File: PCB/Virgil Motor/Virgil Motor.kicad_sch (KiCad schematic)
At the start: 14 parts, among them J1 10056847-101LF, J2 Conn_01x04_Pin, U1 B103, U2 DRV8220DSG, U3 IQS227B00400008TSR, U5 XIAO-RP2350-SMD

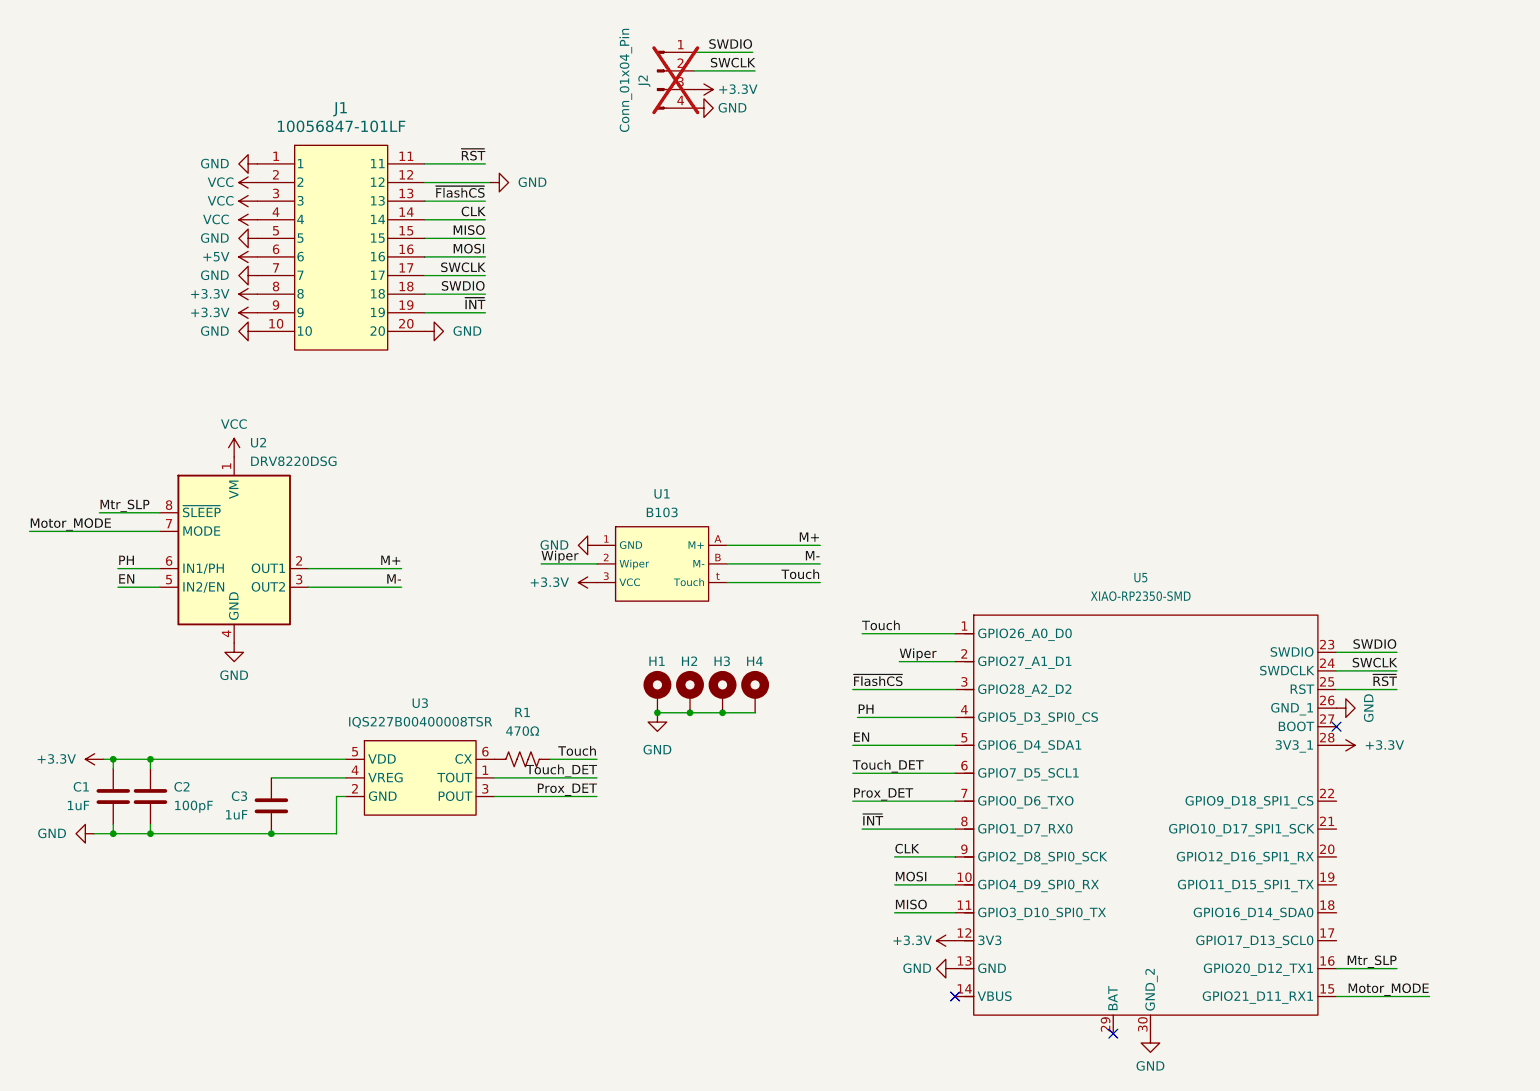
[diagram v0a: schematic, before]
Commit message: Updated PCBs to use raw rp2040s
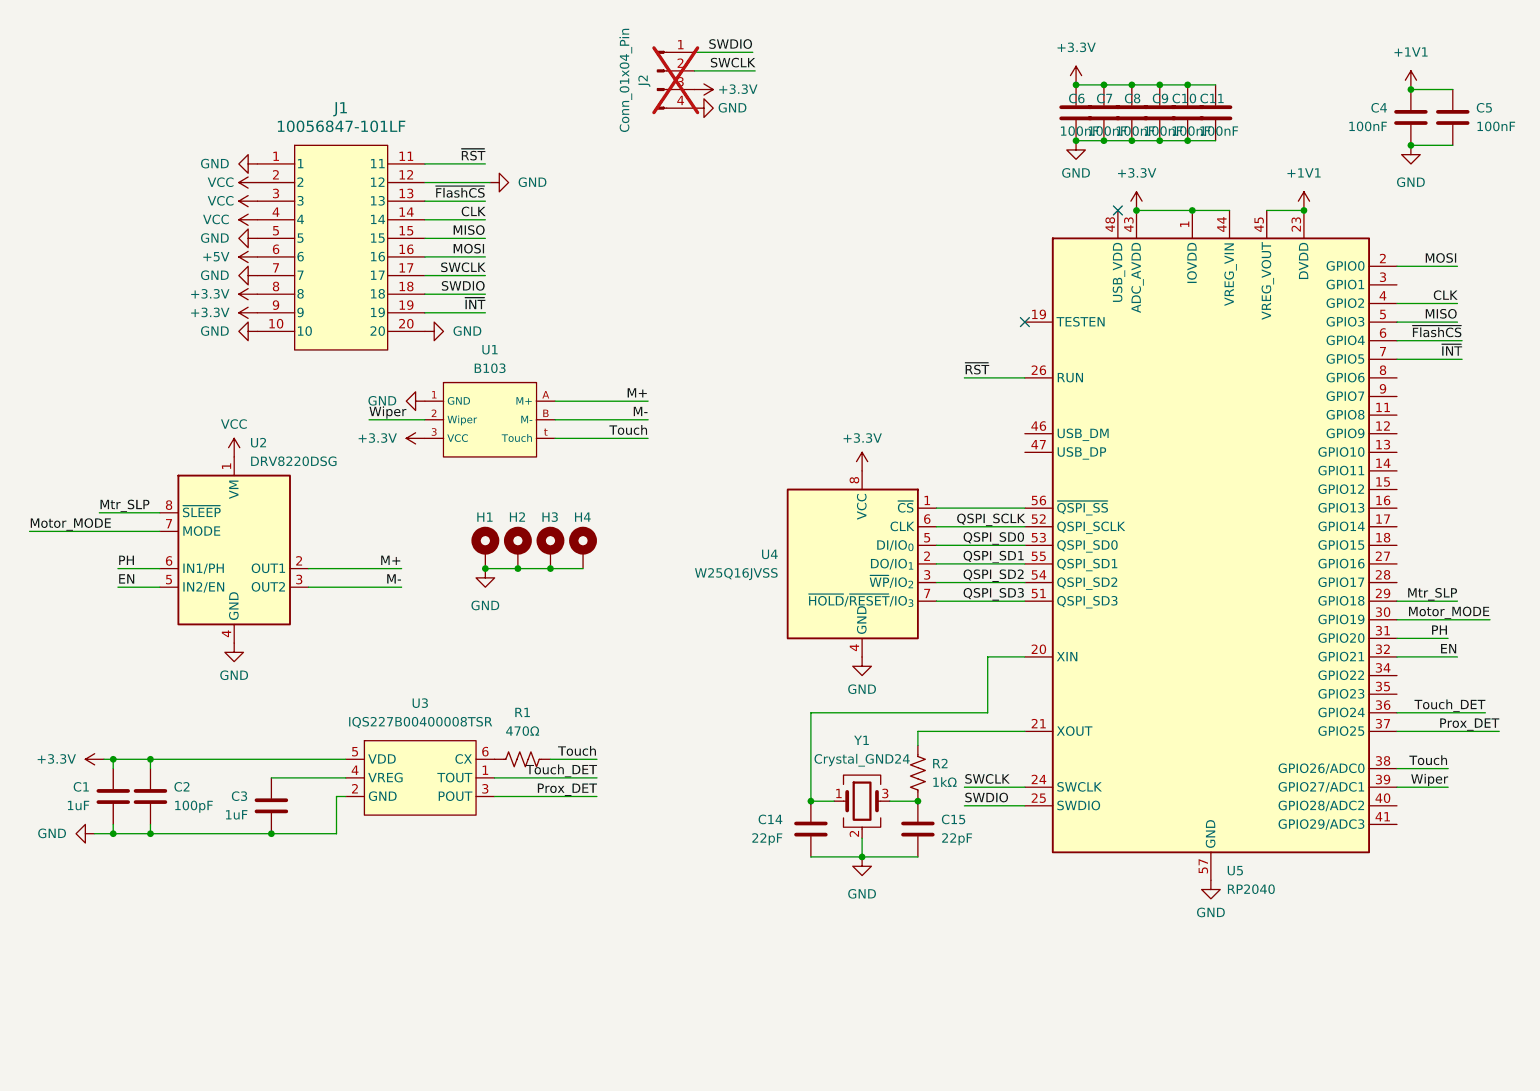
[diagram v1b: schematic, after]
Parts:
- removed U5: XIAO-RP2350-SMD, Snapeda:XIAO-RP2350-SMD, symbol Snapeda:XIAO-RP2350-SMD
- added C10, C11, C4, C5, C6, C7, C8, C9: 100nF, Capacitor_SMD:C_0603_1608Metric, symbol Device:C
- added C14, C15: 22pF, Capacitor_SMD:C_0603_1608Metric, symbol Device:C
- added R2: 1kΩ, Resistor_SMD:R_0603_1608Metric, symbol Device:R_US
- added U4: W25Q16JVSS, Package_SO:SOIC-8_5.3x5.3mm_P1.27mm, symbol Memory_Flash:W25Q16JVSS
- added U5: RP2040, Package_DFN_QFN:QFN-56-1EP_7x7mm_P0.4mm_EP3.2x3.2mm, symbol MCU_RaspberryPi:RP2040
- added Y1: Crystal_GND24, Crystal:Crystal_SMD_Abracon_ABM8G-4Pin_3.2x2.5mm, symbol Device:Crystal_GND24
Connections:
- net +3.3V: now also C10.1, C11.1, C6.1, C7.1, C8.1, C9.1, U4.8 (VCC), U5.1 (IOVDD), U5.10 (IOVDD), U5.22 (IOVDD), U5.33 (IOVDD), U5.42 (IOVDD), U5.43 (ADC_AVDD), U5.44 (VREG_VIN), U5.49 (IOVDD)
- net CLK: now also U5.4 (GPIO2)
- net EN: now also U5.32 (GPIO21)
- net GND: now also C10.2, C11.2, C14.1, C15.1, C4.2, C5.2, C6.2, C7.2, C8.2, C9.2, U4.4 (GND), U5.57 (GND), Y1.2 (G), Y1.4 (G)
- net MISO: now also U5.5 (GPIO3)
- net MOSI: now also U5.2 (GPIO0)
- net Motor_MODE: now also U5.30 (GPIO19)
- net Mtr_SLP: now also U5.29 (GPIO18)
- net PH: now also U5.31 (GPIO20)
- net Prox_DET: now also U5.37 (GPIO25)
- net SWCLK: now also U5.24 (SWCLK)
- net SWDIO: now also U5.25 (SWDIO)
- net Touch: now also U5.38 (GPIO26/ADC0)
- net Touch_DET: now also U5.36 (GPIO24)
- net Wiper: now also U5.39 (GPIO27/ADC1)
- net ~{FlashCS}: now also U5.6 (GPIO4)
- net ~{INT}: now also U5.7 (GPIO5)
- net ~{RST}: now also U5.26 (RUN)
- new net: C14.2, U5.20 (XIN), Y1.1
- new net: C15.2, R2.2, Y1.3
- new net: U4.1 (~{CS}), U5.56 (~{QSPI_SS})
- new net: R2.1, U5.21 (XOUT)
- new net +1V1: C4.1, C5.1, U5.23 (DVDD), U5.45 (VREG_VOUT), U5.50 (DVDD)
- new net QSPI_SCLK: U4.6 (CLK), U5.52 (QSPI_SCLK)
- new net QSPI_SD0: U4.5 (DI/IO_{0}), U5.53 (QSPI_SD0)
- new net QSPI_SD1: U4.2 (DO/IO_{1}), U5.55 (QSPI_SD1)
- new net QSPI_SD2: U4.3 (~{WP}/IO_{2}), U5.54 (QSPI_SD2)
- new net QSPI_SD3: U4.7 (~{HOLD}/~{RESET}/IO_{3}), U5.51 (QSPI_SD3)
- no-connect marks 3 -> 2
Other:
- moved on the sheet: H1, H2, H3, H4, U1

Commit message: Finished PCBs
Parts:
- J1, U1: now not fitted
- Y1: value Crystal_GND24 -> ABM8-272-T3
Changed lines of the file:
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@@
 			)
 		)
-		(property "Value" "Crystal_GND24"
+		(property "Value" "ABM8-272-T3"
 			(at 174.625 115.57 0)
 			(show_name no)
@@
 		(on_board yes)
 		(in_pos_files yes)
-		(dnp no)
+		(dnp yes)
 		(fields_autoplaced yes)
 		(property "Reference" "U1"
@@
 		(on_board yes)
 		(in_pos_files yes)
-		(dnp no)
+		(dnp yes)
 		(fields_autoplaced yes)
 		(property "Reference" "J1"

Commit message: Added Images to readme
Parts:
- removed C1, C3: 1uF, Capacitor_SMD:C_0805_2012Metric, symbol Device:C
- removed C2: 100pF, Capacitor_SMD:C_0805_2012Metric, symbol Device:C
- removed R1: 470Ω, Resistor_SMD:R_0805_2012Metric, symbol Device:R_US
- removed U3: IQS227B00400008TSR, Package_TO_SOT_SMD:TSOT-23-6, symbol Snapeda:IQS227B00400008TSR
- added U3: CAP1293-1-SN-TR, Snapeda:SOIC8_4P9X3P9MC_MCH-L, symbol Snapeda:CAP1293-1-SN-TR
- C14, C15: value 22pF -> 15pF
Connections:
- net +3.3V: now also U3.4 (VDD)
- net GND: now also U3.5 (GND)
- net Touch: now also U3.6 (CS3), U3.7 (CS2/SG), U3.8 (CS1)
- net Touch_INT: now reaches U5.35 (GPIO23)
- net Touch_INT: now also U3.1 (ALERT-)
- net Prox_DET renamed SCL
- net SCL: now also U3.3 (SMCLK)
- net Touch_DET renamed SDA
- net SDA: now also U3.2 (SMDAT)
